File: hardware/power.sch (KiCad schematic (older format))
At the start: 75 parts, among them CON2 BARREL_JACK, U18 TPS5420D, U19 TPS5420D, U20 LP5907-3.0, U21 LP2985A-10DBVR, U23 TPS7A91, U24 TPS7A91, U25 MIC5301-3.3

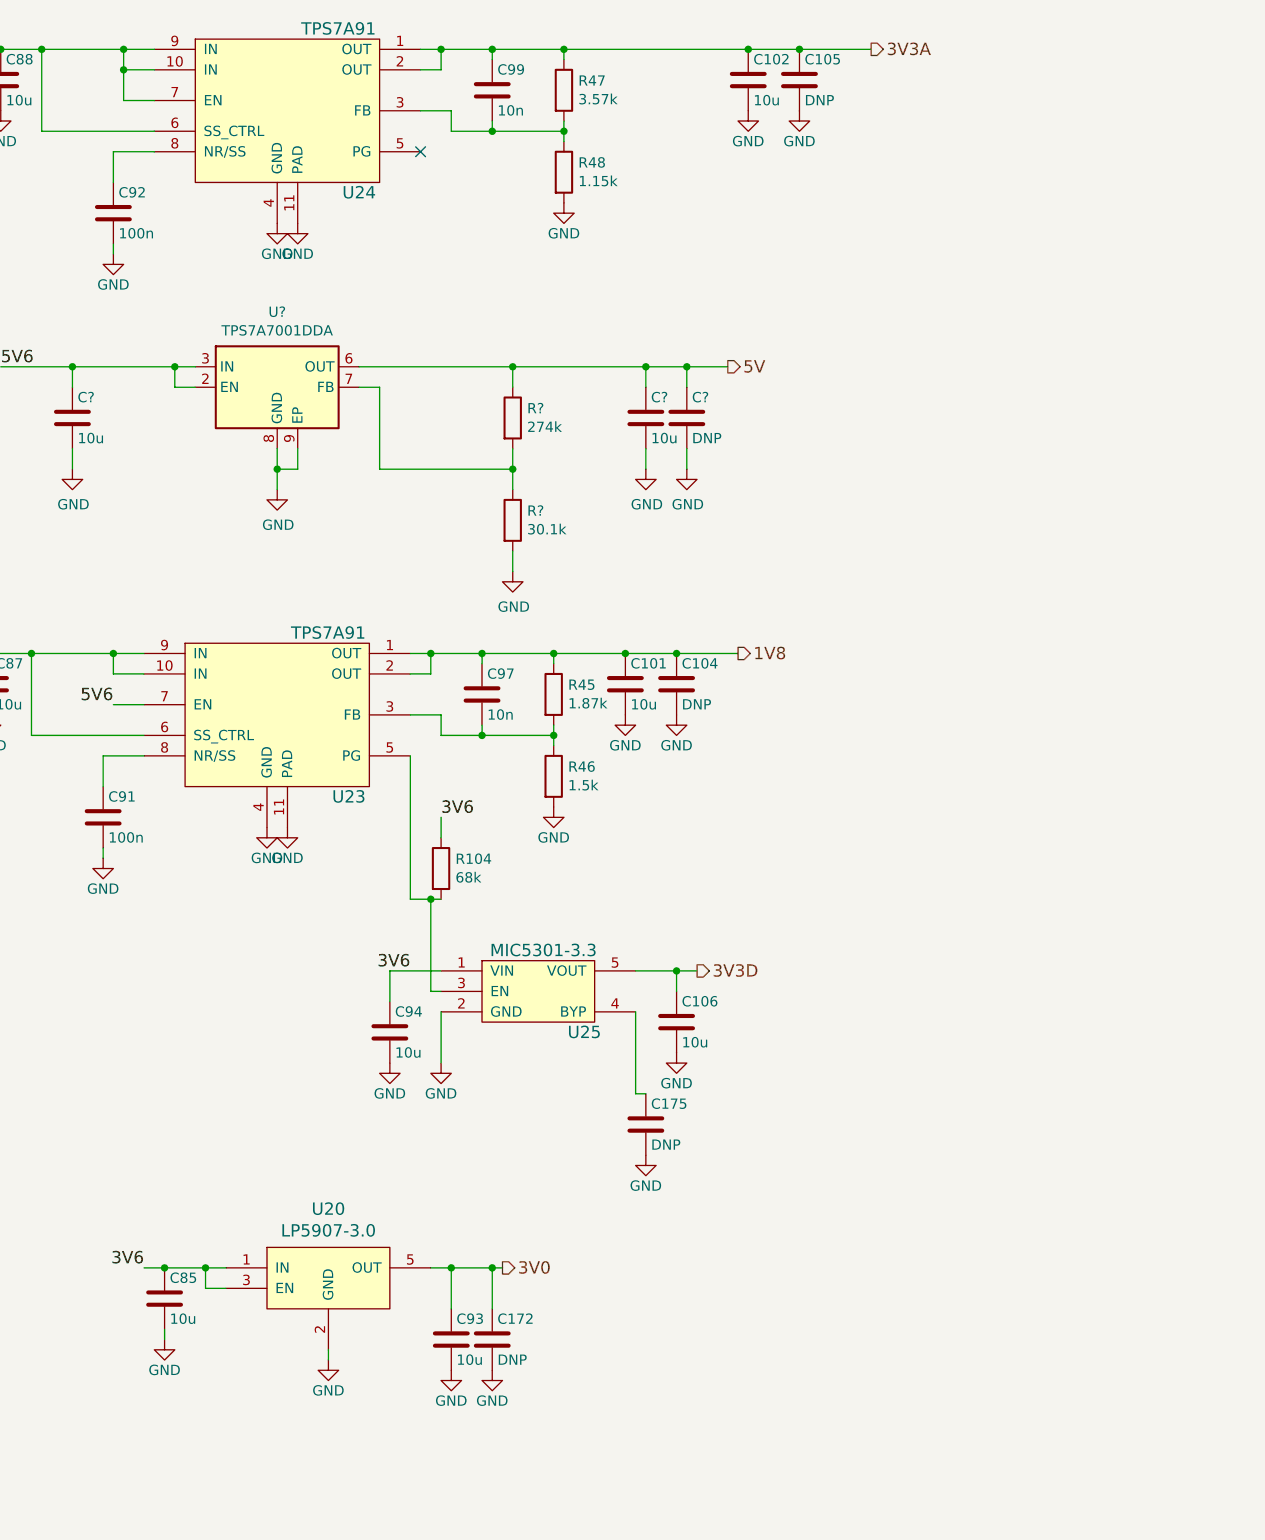
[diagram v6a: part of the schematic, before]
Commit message: Improved top level documentation.
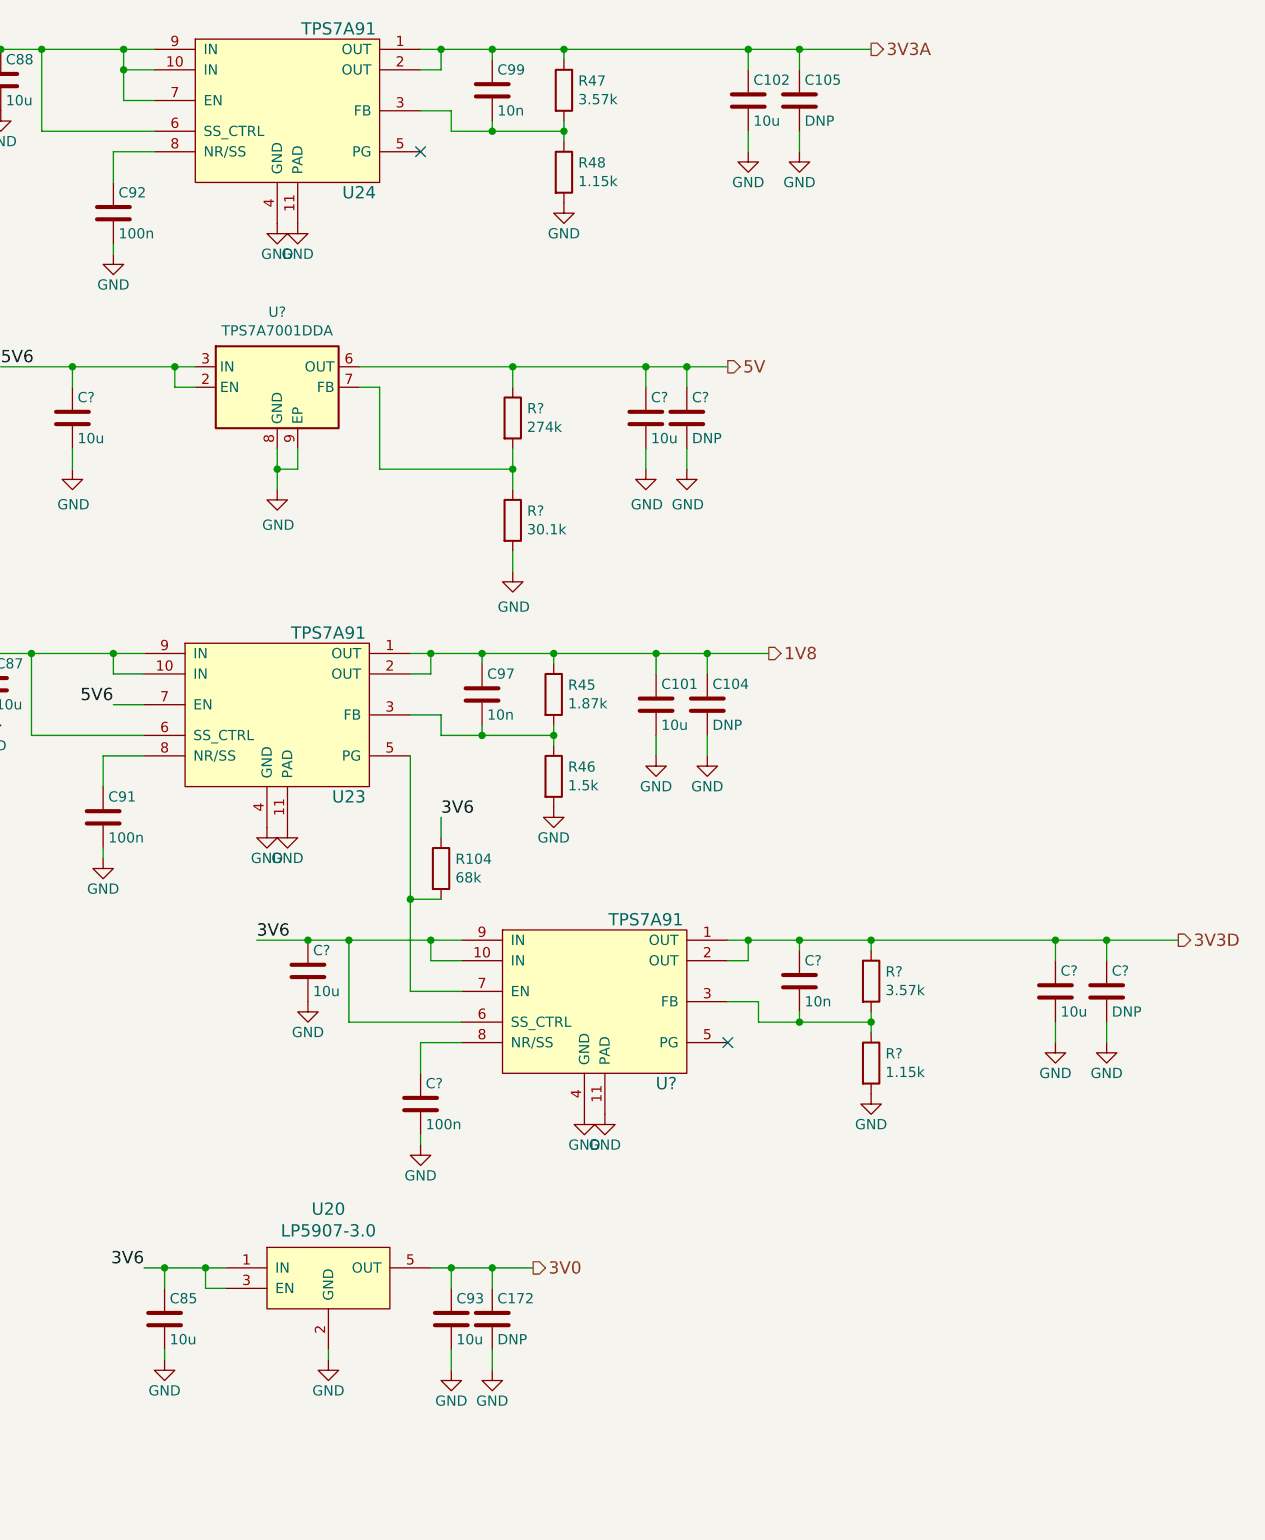
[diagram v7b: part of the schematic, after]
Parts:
- removed C106, C94: 10u, Capacitor_SMD:C_0805_2012Metric, symbol Device:C
- removed C175: DNP, Capacitor_SMD:C_0402_1005Metric, symbol Device:C
- removed U25: MIC5301-3.3, Package_TO_SOT_SMD:SOT-23-5, symbol fmcw-rescue:MIC5301-fmcw3-rescue
- added C? (x2): 10u, Capacitor_SMD:C_0805_2012Metric, symbol Device:C
- added C?: DNP, Capacitor_SMD:C_0805_2012Metric, symbol Device:C
- added C?: 100n, Capacitor_SMD:C_0402_1005Metric, symbol Device:C
- added C?: 10n, Capacitor_SMD:C_0402_1005Metric, symbol Device:C
- added R?: 3.57k, fmcw:R_0402b, symbol Device:R
- added R?: 1.15k, fmcw:R_0402b, symbol Device:R
- added U?: TPS7A91, fmcw:SON-10_2.5x2.5mm, symbol fmcw-rescue:TPS7A91-fmcw3-rescue
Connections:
- net 3V3D: now also C?.1, C?.1, C?.1, R?.1, U?.1 (OUT), U?.2 (OUT)
- net 3V6: now also C?.1, U?.10 (IN), U?.6 (SS_CTRL), U?.9 (IN)
- net GND: now also C?.2, C?.2, C?.2, C?.2, R?.2, U?.11 (PAD), U?.4 (GND)
- net at R104.2, U23.5 (PG): now also U?.7 (EN)
- new net: C?.2, R?.1, R?.2, U?.3 (FB)
- new net: C?.1, U?.8 (NR/SS)
- no-connect marks 4 -> 5
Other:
- moved on the sheet: C101, C102, C104, C105, C172, C85, C93

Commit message: Added MFNs to components.
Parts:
- C100: renamed from C?; MFN (none) -> CL05B104KO5NNNC
- C101, C102, C85, C87, C88, C93: MFN 885012107014 -> CL21B106KQQNNNE
- C103, C175, C94, C96: renamed from C?; MFN 885012107014 -> CL21B106KQQNNNE
- C106: renamed from C?; MFN 885012107014 -> (none)
- C62, C64, C69, C70, C73, C74, C75, C76, C98: MFN GRM21BR61E106MA73L -> CL21B106KQQNNNE
- C79, C80: value 6TPH100MAEA -> 100u; footprint (none) -> Capacitor_Tantalum_SMD:CP_EIA-7343-31_Kemet-D; MFN (none) -> TPSD107M010R0080
- C81, C83, C84, C86, C90: renamed from C?; MFN GRM21BR61E106MA73L -> CL21B106KQQNNNE
- C89: MFN CL10A105KA8NNNC -> CL10B105MO8NNWC
- C91, C92: MFN (none) -> CL05B104KO5NNNC
- C95: MFN (none) -> GRM155R71E103KA01D
- D1: value LED -> Red; footprint Diode_SMD:D_0603_1608Metric -> LED_SMD:LED_0603_1608Metric
- D2, D3: footprint (none) -> Diode_SMD:D_SOD-123F; MFN (none) -> SS24FL
- FB11: footprint Capacitor_SMD:C_0603_1608Metric -> Inductor_SMD:L_0603_1608Metric
- L6: renamed from L?; value 10u -> 33u; footprint (none) -> Inductor_SMD:L_Bourns_SRR1210A; MFN 744777910 -> SRR1210A-330M
- R104: footprint fmcw:R_0402b -> Resistor_SMD:R_0402_1005Metric; MFN (none) -> ERJ-2RKF6802X
- R14, R25: footprint (none) -> Resistor_SMD:R_0402_1005Metric; MFN (none) -> ERJ-2RKF1002X
- R19: footprint (none) -> Resistor_SMD:R_0402_1005Metric; MFN (none) -> ERA-2AEB5111X
- R26: footprint (none) -> Resistor_SMD:R_0402_1005Metric; MFN (none) -> ERJ-2RKF2801X
- R28: renamed from R?; footprint (none) -> Resistor_SMD:R_0402_1005Metric; MFN (none) -> ERJ-2RKF4991X
- R29: renamed from R?; footprint (none) -> Resistor_SMD:R_0402_1005Metric; MFN (none) -> ERJ-2RKF2002X
- R30: renamed from R?; footprint fmcw:R_0402b -> Resistor_SMD:R_0402_1005Metric; MFN (none) -> ERJ-2RKF2743X
- R31: renamed from R?; footprint fmcw:R_0402b -> Resistor_SMD:R_0402_1005Metric; MFN (none) -> ERJ-2RKF3012X
- R32: renamed from R?; footprint fmcw:R_0402b -> Resistor_SMD:R_0402_1005Metric; MFN (none) -> ERJ-2RKF3571X
- R33: renamed from R?; footprint fmcw:R_0402b -> Resistor_SMD:R_0402_1005Metric; MFN (none) -> ERJ-2RKF1151X
- R45: footprint fmcw:R_0402b -> Resistor_SMD:R_0402_1005Metric; MFN (none) -> ERJ-2RKF1871X
- R46: footprint fmcw:R_0402b -> Resistor_SMD:R_0402_1005Metric; MFN (none) -> ERJ-2RKF1501X
- R47: footprint fmcw:R_0402b -> Resistor_SMD:R_0402_1005Metric; MFN (none) -> ERJ-2RKF3571X
- R48: footprint fmcw:R_0402b -> Resistor_SMD:R_0402_1005Metric; MFN (none) -> ERJ-2RKF1151X
- U18, U19: MFN TPS5420D -> TPS5420DR
- U21: footprint fmcw3:SOT-23-5 -> Package_TO_SOT_SMD:SOT-23-5
- U22: renamed from U?; MFN (none) -> TPS560200DBVR
- U25: renamed from U?; MFN (none) -> TPS7A7001DDAR
- gave numbers to parts that had none: 4
